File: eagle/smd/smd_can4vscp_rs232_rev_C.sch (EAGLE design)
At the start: 31 parts, among them IC1 PIC18F2580, IC3 MCP2551SN, IC4 LM2575S, IC7 ST232B (0.1uF)/MAX232IDWR (1u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, J2 A00-108-220-450, Q1 HC-49S

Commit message: Added switches for RS-232/TTL
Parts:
- added J5, J6: (no value), con-lstb:MA03-1
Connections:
- new net RXIF: IC7G$1.R1OUT, J5.3
- new net RXTTL: J3.2, J5.1
- new net TXIF: IC7G$1.T1IN, J6.3
- new net TXTTL: J3.3, J6.1
- net RX: now also J5.2; no longer IC7G$1.R1OUT, J3.2
- net TX: now also J6.2; no longer IC7G$1.T1IN, J3.3

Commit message: All verbose commands now return +OK
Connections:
- net GND: now also J4.5; no longer J4.1
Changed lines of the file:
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@@
 </segment>
 <segment>
-<wire x1="58.42" y1="91.44" x2="58.42" y2="119.38" width="0.1524" layer="91"/>
-<wire x1="58.42" y1="119.38" x2="81.28" y2="119.38" width="0.1524" layer="91"/>
+<wire x1="58.42" y1="91.44" x2="58.42" y2="109.22" width="0.1524" layer="91"/>
 <pinref part="GND1" gate="1" pin="GND"/>
-<pinref part="J4" gate="G$1" pin="1"/>
+<pinref part="J4" gate="G$1" pin="5"/>
+<wire x1="81.28" y1="109.22" x2="58.42" y2="109.22" width="0.1524" layer="91"/>
 </segment>
 <segment>

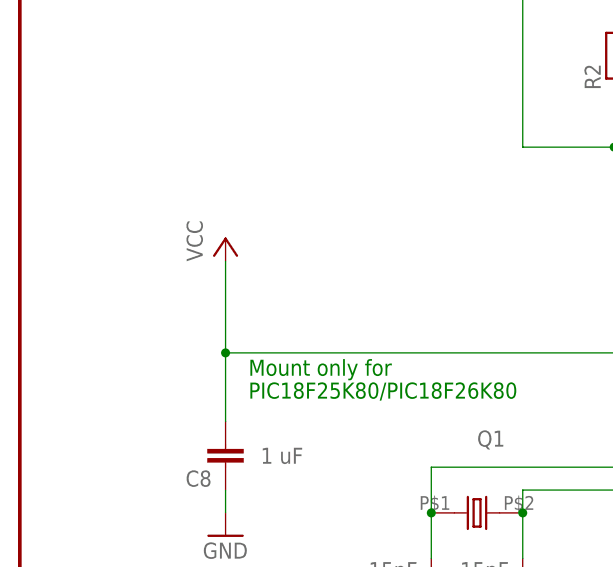
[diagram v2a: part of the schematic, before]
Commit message: Removed VCC from VCAP.
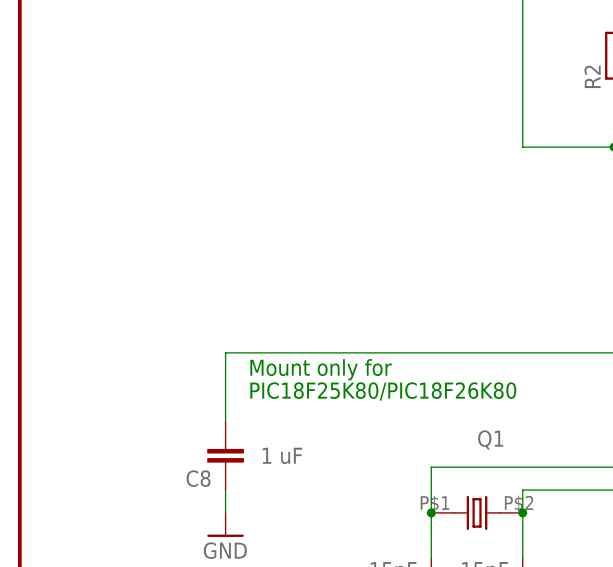
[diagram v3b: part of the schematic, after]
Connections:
- new net N$8: C8.2, IC1.RA4/T0CKIN
- net VCC: no longer C8.2, IC1.RA4/T0CKIN
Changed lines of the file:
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@@
 <part name="PAD1" library="wirepad" deviceset="1,6/0,8" device=""/>
 <part name="PAD2" library="wirepad" deviceset="1,6/0,8" device=""/>
-<part name="P+4" library="SUPPLY1" deviceset="VCC" device=""/>
 <part name="C7" library="cap-master" deviceset="CNP-" device="0805" value="100nF"/>
 <part name="GND18" library="SUPPLY1" deviceset="GND" device=""/>
@@
 <instance part="PAD1" gate="P" x="233.68" y="246.38"/>
 <instance part="PAD2" gate="P" x="233.68" y="238.76"/>
-<instance part="P+4" gate="VCC" x="22.86" y="215.9"/>
 <instance part="C7" gate="G$1" x="152.4" y="25.4" rot="R90"/>
 <instance part="GND18" gate="1" x="152.4" y="20.32"/>
@@
 <junction x="144.78" y="33.02"/>
 </segment>
-<segment>
-<wire x1="22.86" y1="203.2" x2="22.86" y2="195.58" width="0.1524" layer="91"/>
-<wire x1="81.28" y1="203.2" x2="22.86" y2="203.2" width="0.1524" layer="91"/>
-<pinref part="C8" gate="G$1" pin="2"/>
-<pinref part="IC1" gate="G$1" pin="RA4/T0CKIN"/>
-<pinref part="P+4" gate="VCC" pin="VCC"/>
-<wire x1="22.86" y1="203.2" x2="22.86" y2="213.36" width="0.1524" layer="91"/>
-<junction x="22.86" y="203.2"/>
-</segment>
 </net>
 <net name="GND" class="0">
@@
 </segment>
 </net>
+<net name="N$8" class="0">
+<segment>
+<wire x1="22.86" y1="203.2" x2="22.86" y2="195.58" width="0.1524" layer="91"/>
+<wire x1="81.28" y1="203.2" x2="22.86" y2="203.2" width="0.1524" layer="91"/>
+<pinref part="C8" gate="G$1" pin="2"/>
+<pinref part="IC1" gate="G$1" pin="RA4/T0CKIN"/>
+</segment>
+</net>

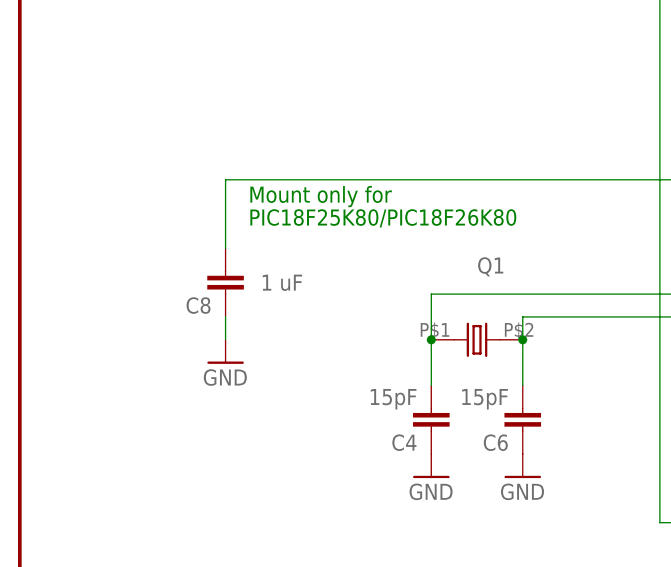
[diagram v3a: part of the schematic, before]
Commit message: RA4 set to input to prevent collision with VCAP circuits in PIC18F2580. Brown out raised to maximum (3V & 4.6V). Valuable input from Anders Forsgren, AJE Electronics AB.
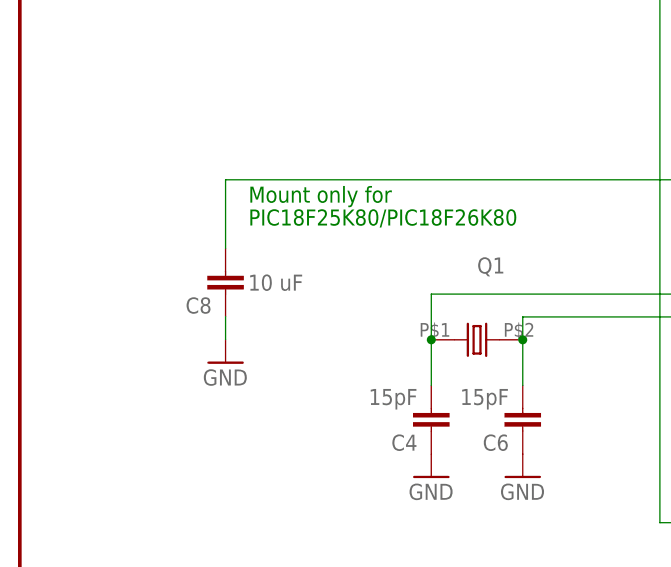
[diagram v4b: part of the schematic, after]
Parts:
- C8: value 1 uF -> 10 uF
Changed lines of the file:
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@@
 <part name="P+2" library="SUPPLY1" deviceset="+12V" device=""/>
 <part name="GND11" library="SUPPLY1" deviceset="GND" device=""/>
-<part name="C8" library="rcl" deviceset="C-EU" device="C0805" value="1 uF"/>
+<part name="C8" library="rcl" deviceset="C-EU" device="C0805" value="10 uF"/>
 <part name="GND17" library="SUPPLY1" deviceset="GND" device=""/>
 <part name="R17" library="rcl" deviceset="R-EU_" device="R0805" value="120"/>
